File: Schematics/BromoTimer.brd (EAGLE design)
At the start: 49.2 x 71.1 mm, 27 parts, among them IC1 PIC16F687, IC2 7805TV, K1 351, K2 351, Q1 2N3565, Q2 2N3565, Q3 2N3565, X4 22-23-2031

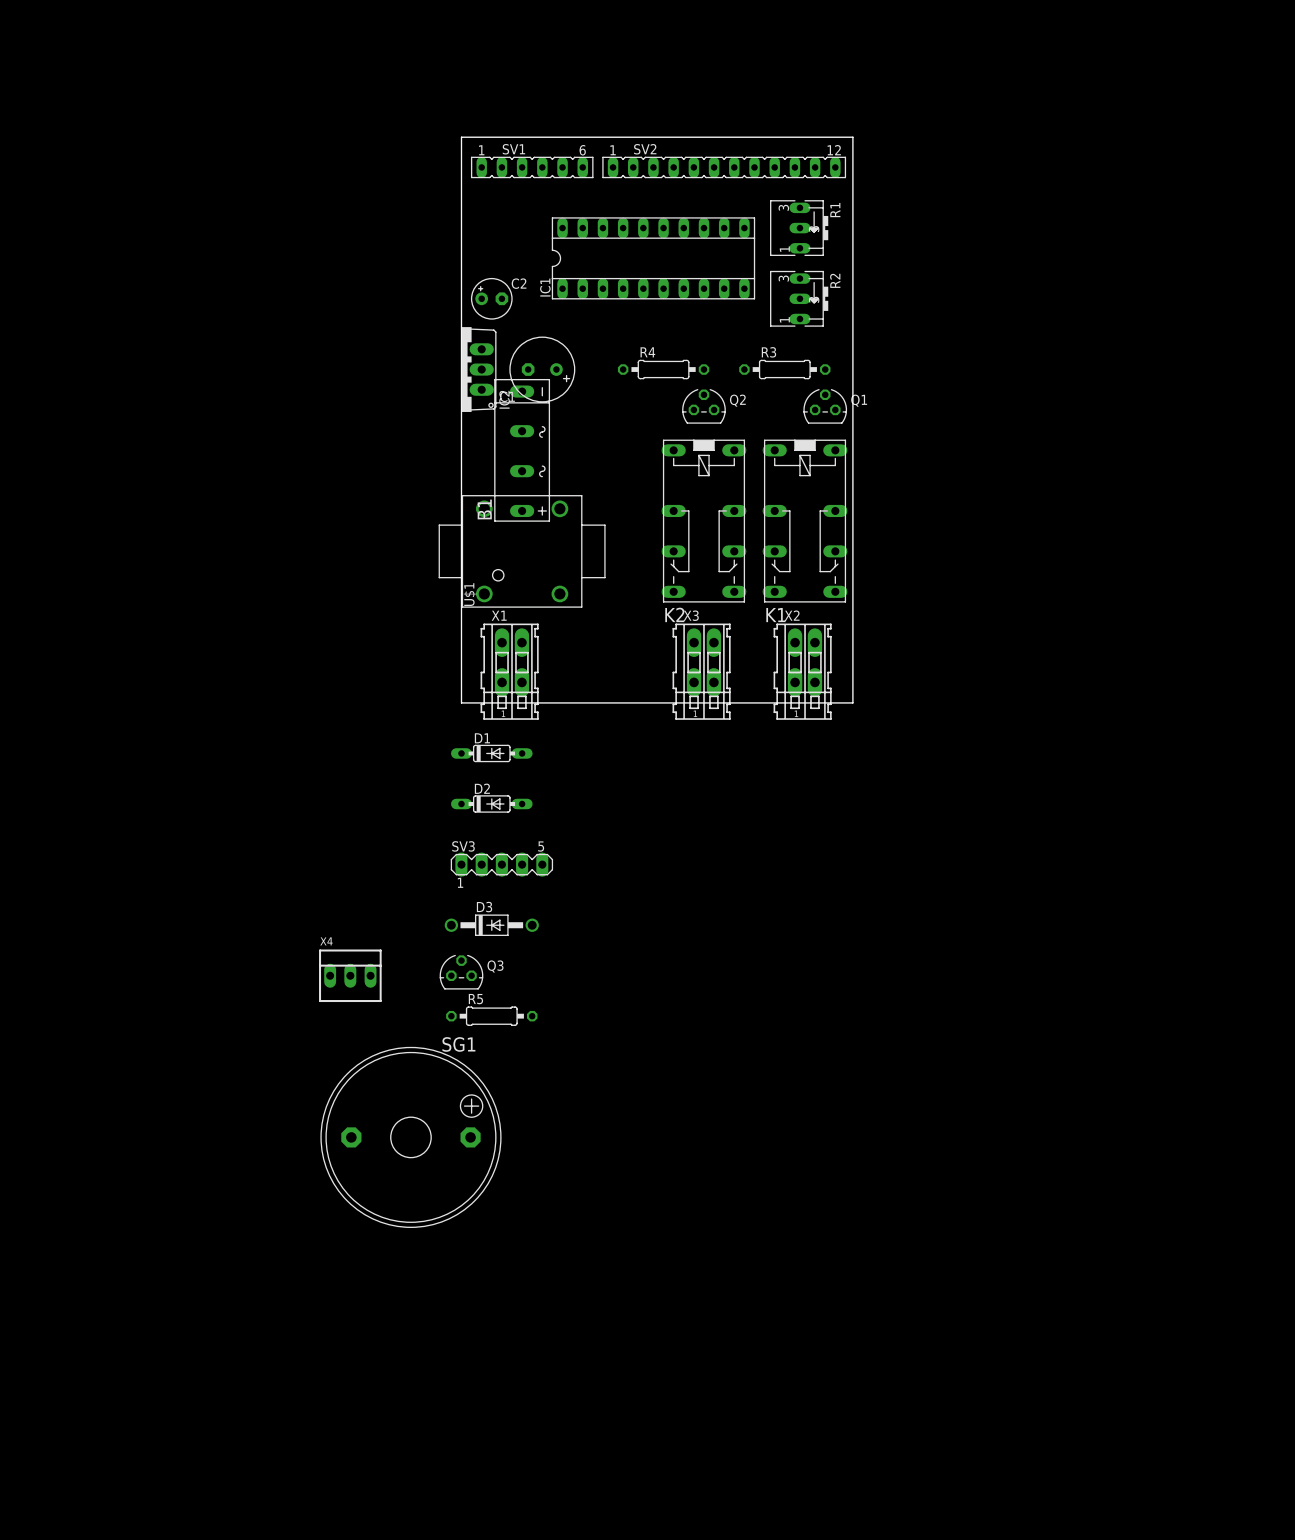
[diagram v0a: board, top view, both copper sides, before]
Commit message: Fixed footprints, added resistor for main led.
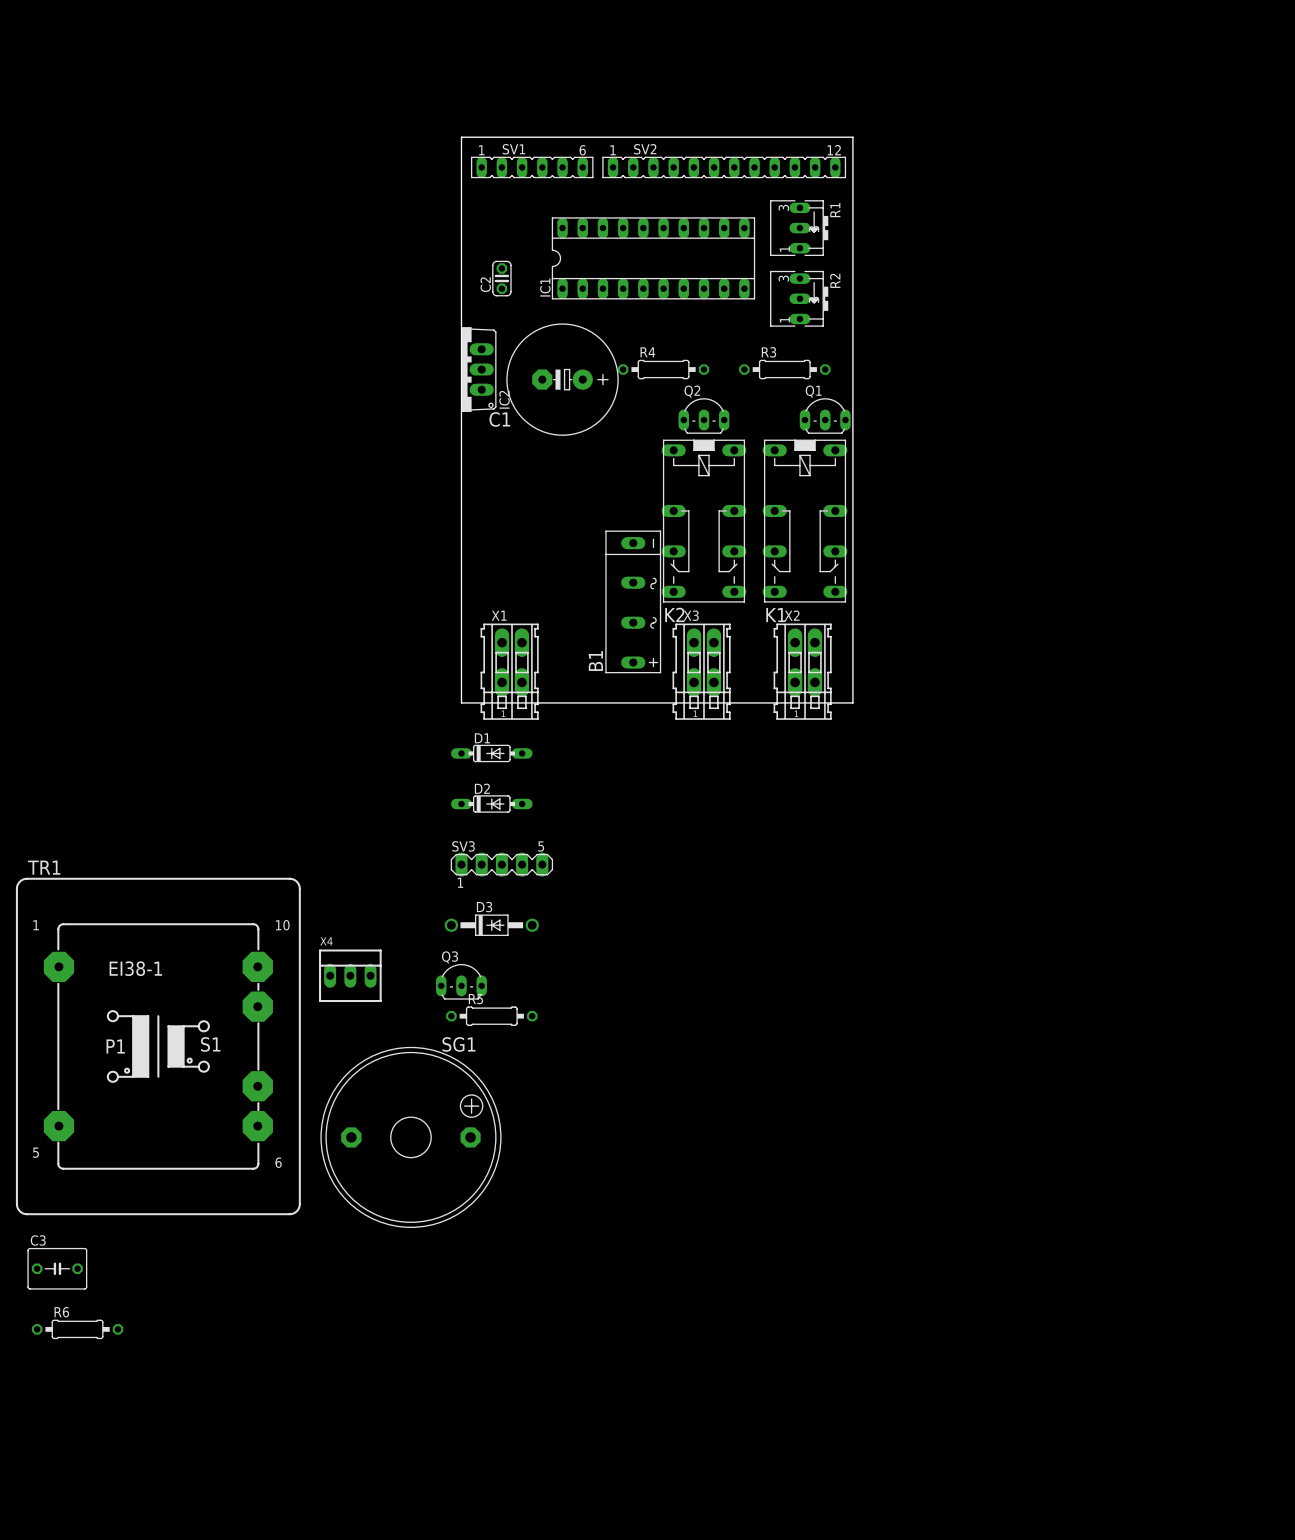
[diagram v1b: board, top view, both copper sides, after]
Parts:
- removed U$1: TRANSFORMERPTH, SparkFun:TRANSFORMER
- added C3: (no value), rcl:C050-050X075
- added R6: (no value), rcl:0207/10
- added TR1: (no value), trafo:EI38-1
- C1: value (none) -> 1m; device rcl:E3,5-8 -> rcl:E5-13
- C2: value (none) -> 100n; device rcl:E2,5-5 -> rcl:C025-024X044
- Q1, Q2, Q3: value 2N3565 -> BC548B; device transistor-npn:TO92 -> transistor-npn:TO92-EBC
- moved B1 23.6 mm to (21.6, 12.7)
- moved C2 2.84 mm to (5.08, 53.3), turned to 90 degrees
- moved C1 2.84 mm to (12.7, 40.6)
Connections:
- new net N$21: R6.2, X4.1
- net +5V: now also C2.1; no longer C2.+
- net AC1: no longer U$1.2
- net AC2: now also TR1.1; no longer U$1.1
- net GND: now also C2.2, C3.2, Q1.E, Q2.E, Q3.E; no longer C2.-, Q1.3, Q2.3, Q3.3
- net N$12: no longer U$1.4
- net N$18: now also Q3.B; no longer Q3.2
- net N$19: now also Q3.C; no longer Q3.1
- net N$2: no longer U$1.3
- net N$20: now also R6.1; no longer X4.1
- net N$4: now also Q2.B; no longer Q2.2
- net N$5: now also Q1.B; no longer Q1.2
- net N$6: now also Q2.C; no longer Q2.1
- net N$7: now also Q1.C; no longer Q1.1
- net V+: now also C3.1

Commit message: Better connector pinouts
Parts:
- removed X2, X3: (no value), con-wago:233-102
- added X5: AC_OUT, con-phoenix-508:MKDSN1,5/5-5,08
- X1: value (none) -> AC_IN; device con-wago:233-102 -> con-phoenix-508:MKDSN1,5/3-5,08
- moved X1 104.0 mm to (-43.2, -86.4)
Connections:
- net AC1: now also X1.1; no longer X1.B1
- net AC2: now also X1.3; no longer X1.B2
- net N$10: now also X5.4; no longer X3.B1
- net N$11: now also X5.5; no longer X3.B2
- net N$8: now also X5.1; no longer X2.B1
- net N$9: now also X5.2; no longer X2.A2, X2.B2
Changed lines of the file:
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@@
 <element name="R3" library="rcl" package="0207/10" value="" x="40.64" y="41.91"/>
 <element name="R4" library="rcl" package="0207/10" value="" x="25.4" y="41.91"/>
-<element name="X2" library="con-wago" package="233-102" value="" x="43.18" y="5.08">
-<attribute name="OC_NEWARK" value="28K9044" x="92.71" y="-2.54" size="1.778" layer="27" display="off"/>
-<attribute name="MPN" value="233-102" x="92.71" y="-2.54" size="1.778" layer="27" display="off"/>
-<attribute name="MF" value="" x="92.71" y="-2.54" size="1.778" layer="27" display="off"/>
-<attribute name="OC_FARNELL" value="unknown" x="92.71" y="-2.54" size="1.778" layer="27" display="off"/>
-</element>
-<element name="X3" library="con-wago" package="233-102" value="" x="30.48" y="5.08">
-<attribute name="OC_NEWARK" value="28K9044" x="87.63" y="-2.54" size="1.778" layer="27" display="off"/>
-<attribute name="MPN" value="233-102" x="87.63" y="-2.54" size="1.778" layer="27" display="off"/>
-<attribute name="MF" value="" x="87.63" y="-2.54" size="1.778" layer="27" display="off"/>
-<attribute name="OC_FARNELL" value="unknown" x="87.63" y="-2.54" size="1.778" layer="27" display="off"/>
-</element>
-<element name="X1" library="con-wago" package="233-102" value="" x="6.35" y="5.08">
-<attribute name="OC_NEWARK" value="28K9044" x="48.26" y="-2.54" size="1.778" layer="27" display="off"/>
-<attribute name="MPN" value="233-102" x="48.26" y="-2.54" size="1.778" layer="27" display="off"/>
-<attribute name="MF" value="" x="48.26" y="-2.54" size="1.778" layer="27" display="off"/>
-<attribute name="OC_FARNELL" value="unknown" x="48.26" y="-2.54" size="1.778" layer="27" display="off"/>
-</element>
 <element name="K1" library="relay" package="351" value="351" x="43.18" y="27.94" rot="R270">
 <attribute name="OC_NEWARK" value="unknown" x="15.24" y="-31.75" size="1.778" layer="27" rot="R270" display="off"/>
@@
 <element name="C3" library="rcl" package="C050-050X075" value="" x="-50.8" y="-71.12"/>
 <element name="R6" library="rcl" package="0207/10" value="" x="-48.26" y="-78.74"/>
+<element name="X1" library="con-phoenix-508" package="MKDSN1,5/3-5,08" value="AC_IN" x="-43.18" y="-86.36">
+<attribute name="OC_NEWARK" value="70R0299" x="-43.18" y="-86.36" size="1.778" layer="27" display="off"/>
+<attribute name="MPN" value="SMKDSN1,5/3-5,08" x="-43.18" y="-86.36" size="1.778" layer="27" display="off"/>
+<attribute name="MF" value="" x="-43.18" y="-86.36" size="1.778" layer="27" display="off"/>
+<attribute name="OC_FARNELL" value="1792904" x="-43.18" y="-86.36" size="1.778" layer="27" display="off"/>
+</element>
+<element name="X5" library="con-phoenix-508" package="MKDSN1,5/5-5,08" value="AC_OUT" x="-40.64" y="-99.06">
+<attribute name="OC_NEWARK" value="70R0301" x="-40.64" y="-99.06" size="1.778" layer="27" display="off"/>
+<attribute name="MPN" value="SMKDSN1,5/5-5,08" x="-40.64" y="-99.06" size="1.778" layer="27" display="off"/>
+<attribute name="MF" value="" x="-40.64" y="-99.06" size="1.778" layer="27" display="off"/>
+<attribute name="OC_FARNELL" value="1792906" x="-40.64" y="-99.06" size="1.778" layer="27" display="off"/>
+</element>
 </elements>
 <signals>
@@
 <signal name="N$8">
 <contactref element="K1" pad="S1"/>
-<contactref element="X2" pad="B1"/>
-<wire x1="41.93" y1="2.58" x2="39.37" y2="13.97" width="0" layer="19" extent="1-1"/>
+<contactref element="X5" pad="1"/>
+<wire x1="39.37" y1="13.97" x2="-50.8211" y2="-99.035" width="0" layer="19" extent="1-1"/>
 </signal>
 <signal name="N$9">
-<contactref element="X2" pad="A2"/>
 <contactref element="K1" pad="S2"/>
-<contactref element="X2" pad="B2"/>
-<wire x1="44.43" y1="7.58" x2="46.99" y2="13.97" width="0" layer="19" extent="1-1"/>
-<wire x1="44.43" y1="2.58" x2="44.43" y2="7.58" width="0" layer="19" extent="1-1"/>
+<contactref element="X5" pad="2"/>
+<wire x1="46.99" y1="13.97" x2="-45.7411" y2="-99.035" width="0" layer="19" extent="1-1"/>
 </signal>
 <signal name="N$10">
-<contactref element="X3" pad="B1"/>
 <contactref element="K2" pad="S1"/>
-<wire x1="29.23" y1="2.58" x2="26.67" y2="13.97" width="0" layer="19" extent="1-1"/>
+<contactref element="X5" pad="4"/>
+<wire x1="26.67" y1="13.97" x2="-35.5811" y2="-99.035" width="0" layer="19" extent="1-1"/>
 </signal>
 <signal name="N$11">
-<contactref element="X3" pad="B2"/>
 <contactref element="K2" pad="S2"/>
-<wire x1="31.73" y1="2.58" x2="34.29" y2="13.97" width="0" layer="19" extent="1-1"/>
+<contactref element="X5" pad="5"/>
+<wire x1="34.29" y1="13.97" x2="-30.5011" y2="-99.035" width="0" layer="19" extent="1-1"/>
 </signal>
 <signal name="AC2">
 <contactref element="K1" pad="P1"/>
 <contactref element="K2" pad="P1"/>
-<contactref element="X1" pad="B2"/>
 <contactref element="TR1" pad="1"/>
-<wire x1="7.6" y1="2.58" x2="-50.5968" y2="-33.1724" width="0" layer="19" extent="1-1"/>
-<wire x1="26.67" y1="24.13" x2="7.6" y2="2.58" width="0" layer="19" extent="1-1"/>
+<contactref element="X1" pad="3"/>
+<wire x1="-50.5968" y1="-33.1724" x2="-40.6611" y2="-86.335" width="0" layer="19" extent="1-1"/>
+<wire x1="26.67" y1="24.13" x2="-50.5968" y2="-33.1724" width="0" layer="19" extent="1-1"/>
 <wire x1="39.37" y1="24.13" x2="26.67" y2="24.13" width="0" layer="19" extent="1-1"/>
 </signal>
@@
 <contactref element="K1" pad="P2"/>
 <contactref element="K2" pad="P2"/>
-<contactref element="X1" pad="B1"/>
-<wire x1="34.29" y1="24.13" x2="46.99" y2="24.13" width="0" layer="19" extent="1-1"/>
-<wire x1="5.1" y1="2.58" x2="34.29" y2="24.13" width="0" layer="19" extent="1-1"/>
+<contactref element="X1" pad="1"/>
+<wire x1="34.29" y1="24.13" x2="-50.8211" y2="-86.335" width="0" layer="19" extent="1-1"/>
+<wire x1="46.99" y1="24.13" x2="34.29" y2="24.13" width="0" layer="19" extent="1-1"/>
 </signal>
 <signal name="N$2">

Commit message: Add proper footprint for relays
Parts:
- K1, K2: value 351 -> G2R2A; device relay:351 -> relay:G2R2A
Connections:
- net N$6: now also K2.2; no longer K2.16
- net N$7: now also K1.2; no longer K1.16
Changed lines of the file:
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@@
 <element name="R3" library="rcl" package="0207/10" value="" x="40.64" y="41.91"/>
 <element name="R4" library="rcl" package="0207/10" value="" x="25.4" y="41.91"/>
-<element name="K1" library="relay" package="351" value="351" x="43.18" y="27.94" rot="R270">
-<attribute name="OC_NEWARK" value="unknown" x="15.24" y="-31.75" size="1.778" layer="27" rot="R270" display="off"/>
-<attribute name="MPN" value="" x="15.24" y="-31.75" size="1.778" layer="27" rot="R270" display="off"/>
+<element name="K1" library="relay" package="G2R2A" value="G2R2A" x="43.18" y="27.94" rot="R270">
+<attribute name="OC_NEWARK" value="36M5257" x="15.24" y="-31.75" size="1.778" layer="27" rot="R270" display="off"/>
+<attribute name="MPN" value="G2R-2A-DC24" x="15.24" y="-31.75" size="1.778" layer="27" rot="R270" display="off"/>
 <attribute name="MF" value="" x="15.24" y="-31.75" size="1.778" layer="27" rot="R270" display="off"/>
-<attribute name="OC_FARNELL" value="unknown" x="15.24" y="-31.75" size="1.778" layer="27" rot="R270" display="off"/>
-</element>
-<element name="K2" library="relay" package="351" value="351" x="30.48" y="27.94" rot="R270">
-<attribute name="OC_NEWARK" value="unknown" x="-10.16" y="-3.81" size="1.778" layer="27" rot="R270" display="off"/>
-<attribute name="MPN" value="" x="-10.16" y="-3.81" size="1.778" layer="27" rot="R270" display="off"/>
+<attribute name="OC_FARNELL" value="6985269" x="15.24" y="-31.75" size="1.778" layer="27" rot="R270" display="off"/>
+</element>
+<element name="K2" library="relay" package="G2R2A" value="G2R2A" x="30.48" y="27.94" rot="R270">
+<attribute name="OC_NEWARK" value="36M5257" x="-10.16" y="-3.81" size="1.778" layer="27" rot="R270" display="off"/>
+<attribute name="MPN" value="G2R-2A-DC24" x="-10.16" y="-3.81" size="1.778" layer="27" rot="R270" display="off"/>
 <attribute name="MF" value="" x="-10.16" y="-3.81" size="1.778" layer="27" rot="R270" display="off"/>
-<attribute name="OC_FARNELL" value="unknown" x="-10.16" y="-3.81" size="1.778" layer="27" rot="R270" display="off"/>
+<attribute name="OC_FARNELL" value="6985269" x="-10.16" y="-3.81" size="1.778" layer="27" rot="R270" display="off"/>
 </element>
 <element name="B1" library="rectifier" package="2KBB-R" value="" x="21.59" y="12.7" rot="R90"/>
@@
 <signal name="N$6">
 <contactref element="Q2" pad="C"/>
-<contactref element="K2" pad="16"/>
+<contactref element="K2" pad="2"/>
 <contactref element="D1" pad="A"/>
-<wire x1="34.29" y1="31.75" x2="27.94" y2="35.56" width="0" layer="19" extent="1-1"/>
-<wire x1="7.62" y1="-6.35" x2="34.29" y2="31.75" width="0" layer="19" extent="1-1"/>
+<wire x1="34.29" y1="30.48" x2="27.94" y2="35.56" width="0" layer="19" extent="1-1"/>
+<wire x1="7.62" y1="-6.35" x2="34.29" y2="30.48" width="0" layer="19" extent="1-1"/>
 </signal>
 <signal name="N$7">
 <contactref element="Q1" pad="C"/>
-<contactref element="K1" pad="16"/>
+<contactref element="K1" pad="2"/>
 <contactref element="D2" pad="A"/>
-<wire x1="46.99" y1="31.75" x2="43.18" y2="35.56" width="0" layer="19" extent="1-1"/>
-<wire x1="7.62" y1="-12.7" x2="46.99" y2="31.75" width="0" layer="19" extent="1-1"/>
+<wire x1="46.99" y1="30.48" x2="43.18" y2="35.56" width="0" layer="19" extent="1-1"/>
+<wire x1="7.62" y1="-12.7" x2="46.99" y2="30.48" width="0" layer="19" extent="1-1"/>
 </signal>
 <signal name="N$8">
 <contactref element="K1" pad="S1"/>
 <contactref element="X5" pad="1"/>
-<wire x1="39.37" y1="13.97" x2="-50.8211" y2="-99.035" width="0" layer="19" extent="1-1"/>
+<wire x1="46.99" y1="5.4864" x2="-50.8211" y2="-99.035" width="0" layer="19" extent="1-1"/>
 </signal>
 <signal name="N$9">
 <contactref element="K1" pad="S2"/>
 <contactref element="X5" pad="2"/>
-<wire x1="46.99" y1="13.97" x2="-45.7411" y2="-99.035" width="0" layer="19" extent="1-1"/>
+<wire x1="39.497" y1="5.4864" x2="-45.7411" y2="-99.035" width="0" layer="19" extent="1-1"/>
 </signal>
 <signal name="N$10">
 <contactref element="K2" pad="S1"/>
 <contactref element="X5" pad="4"/>
-<wire x1="26.67" y1="13.97" x2="-35.5811" y2="-99.035" width="0" layer="19" extent="1-1"/>
+<wire x1="34.29" y1="5.4864" x2="-35.5811" y2="-99.035" width="0" layer="19" extent="1-1"/>
 </signal>
 <signal name="N$11">
 <contactref element="K2" pad="S2"/>
 <contactref element="X5" pad="5"/>
-<wire x1="34.29" y1="13.97" x2="-30.5011" y2="-99.035" width="0" layer="19" extent="1-1"/>
+<wire x1="26.797" y1="5.4864" x2="-30.5011" y2="-99.035" width="0" layer="19" extent="1-1"/>
 </signal>
 <signal name="AC2">
@@
 <contactref element="X1" pad="3"/>
 <wire x1="-50.5968" y1="-33.1724" x2="-40.6611" y2="-86.335" width="0" layer="19" extent="1-1"/>
-<wire x1="26.67" y1="24.13" x2="-50.5968" y2="-33.1724" width="0" layer="19" extent="1-1"/>
-<wire x1="39.37" y1="24.13" x2="26.67" y2="24.13" width="0" layer="19" extent="1-1"/>
+<wire x1="34.29" y1="10.4902" x2="-50.5968" y2="-33.1724" width="0" layer="19" extent="1-1"/>
+<wire x1="46.99" y1="10.4902" x2="34.29" y2="10.4902" width="0" layer="19" extent="1-1"/>
 </signal>
 <signal name="AC1">
@@
 <contactref element="K2" pad="P2"/>
 <contactref element="X1" pad="1"/>
-<wire x1="34.29" y1="24.13" x2="-50.8211" y2="-86.335" width="0" layer="19" extent="1-1"/>
-<wire x1="46.99" y1="24.13" x2="34.29" y2="24.13" width="0" layer="19" extent="1-1"/>
+<wire x1="26.797" y1="10.4902" x2="-50.8211" y2="-86.335" width="0" layer="19" extent="1-1"/>
+<wire x1="39.497" y1="10.4902" x2="26.797" y2="10.4902" width="0" layer="19" extent="1-1"/>
 </signal>
 <signal name="N$2">
@@
 <wire x1="0" y1="-6.35" x2="0" y2="-12.7" width="0" layer="19" extent="1-1"/>
 <wire x1="21.59" y1="5.08" x2="0" y2="-6.35" width="0" layer="19" extent="1-1"/>
-<wire x1="26.67" y1="31.75" x2="21.59" y2="5.08" width="0" layer="19" extent="1-1"/>
-<wire x1="39.37" y1="31.75" x2="26.67" y2="31.75" width="0" layer="19" extent="1-1"/>
-<wire x1="15.24" y1="40.64" x2="26.67" y2="31.75" width="0" layer="19" extent="1-1"/>
+<wire x1="26.797" y1="30.48" x2="21.59" y2="5.08" width="0" layer="19" extent="1-1"/>
+<wire x1="39.497" y1="30.48" x2="26.797" y2="30.48" width="0" layer="19" extent="1-1"/>
+<wire x1="15.24" y1="40.64" x2="26.797" y2="30.48" width="0" layer="19" extent="1-1"/>
 <wire x1="2.54" y1="39.37" x2="15.24" y2="40.64" width="0" layer="19" extent="1-1"/>
 </signal>
